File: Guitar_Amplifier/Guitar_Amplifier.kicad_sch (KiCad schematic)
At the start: 11 parts, among them J1 Conn_01x04, J2 Conn_01x02, U1 LM386

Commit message: First version of board layout
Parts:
- C1, C2, C4: footprint (none) -> Capacitor_SMD:C_0603_1608Metric
- C3: footprint (none) -> Capacitor_SMD:CP_Elec_10x10
- D1: footprint (none) -> Diode_SMD:D_0805_2012Metric
- J1: footprint (none) -> Connector_PinHeader_1.00mm:PinHeader_1x04_P1.00mm_Vertical
- J2: footprint (none) -> Connector_PinHeader_1.00mm:PinHeader_1x02_P1.00mm_Vertical
- R1, R2: footprint (none) -> Resistor_SMD:R_0603_1608Metric
- RV1: footprint (none) -> Potentiometer_SMD:Potentiometer_Bourns_TC33X_Vertical; Distributor (none) -> Digikey; Distributor PN (none) -> TC33X-103ETR-ND; Mfg. (none) -> Bourns Inc.; Mfg. PN (none) -> TC33X-2-103E
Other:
- moved on the sheet: C1
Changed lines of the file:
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@@
 	)
 	(junction
-		(at 125.73 57.15)
+		(at 125.73 66.04)
 		(diameter 0)
 		(color 0 0 0 0)
@@
 	(wire
 		(pts
-			(xy 134.62 57.15) (xy 134.62 59.69)
+			(xy 134.62 66.04) (xy 134.62 68.58)
 		)
 		(stroke
@@
 	(wire
 		(pts
-			(xy 134.62 67.31) (xy 134.62 71.12)
+			(xy 134.62 76.2) (xy 134.62 80.01)
 		)
 		(stroke
@@
 	(wire
 		(pts
-			(xy 80.01 74.93) (xy 82.55 74.93)
+			(xy 80.01 74.93) (xy 85.09 74.93)
 		)
 		(stroke
@@
 	(wire
 		(pts
-			(xy 125.73 57.15) (xy 134.62 57.15)
+			(xy 125.73 66.04) (xy 134.62 66.04)
 		)
 		(stroke
@@
 	(wire
 		(pts
-			(xy 125.73 52.07) (xy 125.73 57.15)
+			(xy 125.73 60.96) (xy 125.73 66.04)
 		)
 		(stroke
@@
 	(wire
 		(pts
-			(xy 125.73 57.15) (xy 125.73 81.28)
+			(xy 125.73 66.04) (xy 125.73 81.28)
 		)
 		(stroke
@@
 	(wire
 		(pts
-			(xy 82.55 74.93) (xy 82.55 71.12)
+			(xy 85.09 74.93) (xy 85.09 68.58)
 		)
 		(stroke
@@
 			)
 		)
-		(property "Footprint" ""
+		(property "Footprint" "Resistor_SMD:R_0603_1608Metric"
 			(at 75.946 104.394 90)
 			(effects
@@
 	(symbol
 		(lib_id "power:+9V")
-		(at 125.73 52.07 0)
+		(at 125.73 60.96 0)
 		(unit 1)
 		(exclude_from_sim no)
@@
 		(fields_autoplaced yes)
 		(property "Reference" "#PWR02"
+			(at 125.73 64.77 0)
+			(effects
+				(font
+					(size 1.27 1.27)
+				)
+				(hide yes)
+			)
+		)
+		(property "Value" "+9V"
 			(at 125.73 55.88 0)
 			(effects
@@
 					(size 1.27 1.27)
 				)
-				(hide yes)
-			)
-		)
-		(property "Value" "+9V"
-			(at 125.73 46.99 0)
-			(effects
-				(font
-					(size 1.27 1.27)
-				)
 			)
 		)
 		(property "Footprint" ""
-			(at 125.73 52.07 0)
+			(at 125.73 60.96 0)
 			(effects
 				(font
@@
 		)
 		(property "Datasheet" ""
-			(at 125.73 52.07 0)
+			(at 125.73 60.96 0)
 			(effects
 				(font
@@
 		)
 		(property "Description" "Power symbol creates a global label with name \"+9V\""
-			(at 125.73 52.07 0)
+			(at 125.73 60.96 0)
 			(effects
 				(font
@@
 			)
 		)
-		(property "Footprint" ""
+		(property "Footprint" "Potentiometer_SMD:Potentiometer_Bourns_TC33X_Vertical"
 			(at 101.6 86.36 0)
 			(effects
@@
 		)
 		(property "Description" "Potentiometer, US symbol"
+			(at 101.6 86.36 0)
+			(effects
+				(font
+					(size 1.27 1.27)
+				)
+				(hide yes)
+			)
+		)
+		(property "Mfg." "Bourns Inc."
+			(at 101.6 86.36 0)
+			(effects
+				(font
+					(size 1.27 1.27)
+				)
+				(hide yes)
+			)
+		)
+		(property "Mfg. PN" "TC33X-2-103E"
+			(at 101.6 86.36 0)
+			(effects
+				(font
+					(size 1.27 1.27)
+				)
+				(hide yes)
+			)
+		)
+		(property "Distributor" "Digikey"
+			(at 101.6 86.36 0)
+			(effects
+				(font
+					(size 1.27 1.27)
+				)
+				(hide yes)
+			)
+		)
+		(property "Distributor PN" "TC33X-103ETR-ND"
 			(at 101.6 86.36 0)
 			(effects
@@
 			)
 		)
-		(property "Footprint" ""
+		(property "Footprint" "Diode_SMD:D_0805_2012Metric"
 			(at 74.93 114.3 0)
 			(effects
@@
 			)
 		)
-		(property "Footprint" ""
+		(property "Footprint" "Connector_PinHeader_1.00mm:PinHeader_1x04_P1.00mm_Vertical"
 			(at 74.93 77.47 0)
 			(effects
@@
 			)
 		)
-		(property "Footprint" ""
+		(property "Footprint" "Connector_PinHeader_1.00mm:PinHeader_1x02_P1.00mm_Vertical"
 			(at 168.91 88.9 0)
 			(effects
@@
 			)
 		)
-		(property "Footprint" ""
+		(property "Footprint" "Capacitor_SMD:C_0603_1608Metric"
 			(at 143.8148 92.71 0)
 			(effects
@@
 	(symbol
 		(lib_id "power:+9V")
-		(at 82.55 71.12 0)
+		(at 85.09 68.58 0)
 		(unit 1)
 		(exclude_from_sim no)
@@
 		(fields_autoplaced yes)
 		(property "Reference" "#PWR04"
-			(at 82.55 74.93 0)
+			(at 85.09 72.39 0)
 			(effects
 				(font
@@
 		)
 		(property "Value" "+9V"
-			(at 82.55 66.04 0)
+			(at 85.09 63.5 0)
 			(effects
 				(font
@@
 		)
 		(property "Footprint" ""
-			(at 82.55 71.12 0)
+			(at 85.09 68.58 0)
 			(effects
 				(font
@@
 		)
 		(property "Datasheet" ""
-			(at 82.55 71.12 0)
+			(at 85.09 68.58 0)
 			(effects
 				(font
@@
 		)
 		(property "Description" "Power symbol creates a global label with name \"+9V\""
-			(at 82.55 71.12 0)
+			(at 85.09 68.58 0)
 			(effects
 				(font
@@
 	(symbol
 		(lib_id "Device:C")
-		(at 134.62 63.5 0)
+		(at 134.62 72.39 0)
 		(unit 1)
 		(exclude_from_sim no)
@@
 		(fields_autoplaced yes)
 		(property "Reference" "C1"
-			(at 138.43 62.2299 0)
+			(at 138.43 71.1199 0)
 			(effects
 				(font
@@
 		)
 		(property "Value" "0.1uF"
-			(at 138.43 64.7699 0)
+			(at 138.43 73.6599 0)
 			(effects
 				(font
@@
 			)
 		)
-		(property "Footprint" ""
-			(at 135.5852 67.31 0)
+		(property "Footprint" "Capacitor_SMD:C_0603_1608Metric"
+			(at 135.5852 76.2 0)
 			(effects
 				(font
@@
 		)
 		(property "Datasheet" "~"
-			(at 134.62 63.5 0)
+			(at 134.62 72.39 0)
 			(effects
 				(font
@@
 		)
 		(property "Description" "CAP CER 0.1UF 25V X7R 0603"
-			(at 134.62 63.5 0)
+			(at 134.62 72.39 0)
 			(effects
 				(font
@@
 		)
 		(property "Mfg." "Samsung Electro-Mechanics"
-			(at 134.62 63.5 0)
+			(at 134.62 72.39 0)
 			(effects
 				(font
@@
 		)
 		(property "Mfg. PN" "CL10B104KA8NNNC"
-			(at 134.62 63.5 0)
+			(at 134.62 72.39 0)
 			(effects
 				(font
@@
 		)
 		(property "Distributor" "Digikey"
-			(at 134.62 63.5 0)
+			(at 134.62 72.39 0)
 			(effects
 				(font
@@
 		)
 		(property "Distributor PN" "1276-1006-2-ND"
-			(at 134.62 63.5 0)
+			(at 134.62 72.39 0)
 			(effects
 				(font
@@
 			)
 		)
-		(property "Footprint" ""
+		(property "Footprint" "Resistor_SMD:R_0603_1608Metric"
 			(at 145.796 108.204 90)
 			(effects
@@
 			)
 		)
-		(property "Footprint" ""
+		(property "Footprint" "Capacitor_SMD:CP_Elec_10x10"
 			(at 154.94 88.9 0)
 			(effects
@@
 	(symbol
 		(lib_id "power:GND")
-		(at 134.62 71.12 0)
+		(at 134.62 80.01 0)
 		(unit 1)
 		(exclude_from_sim no)
@@
 		(fields_autoplaced yes)
 		(property "Reference" "#PWR07"
-			(at 134.62 77.47 0)
+			(at 134.62 86.36 0)
 			(effects
 				(font
@@
 		)
 		(property "Value" "GND"
-			(at 134.62 76.2 0)
+			(at 134.62 85.09 0)
 			(effects
 				(font
@@
 		)
 		(property "Footprint" ""
-			(at 134.62 71.12 0)
+			(at 134.62 80.01 0)
 			(effects
 				(font
@@
 		)
 		(property "Datasheet" ""
-			(at 134.62 71.12 0)
+			(at 134.62 80.01 0)
 			(effects
 				(font
@@
 		)
 		(property "Description" "Power symbol creates a global label with name \"GND\" , ground"
-			(at 134.62 71.12 0)
+			(at 134.62 80.01 0)
 			(effects
 				(font
@@
 			)
 		)
-		(property "Footprint" ""
+		(property "Footprint" "Capacitor_SMD:C_0603_1608Metric"
 			(at 134.62 110.7948 0)
 			(effects

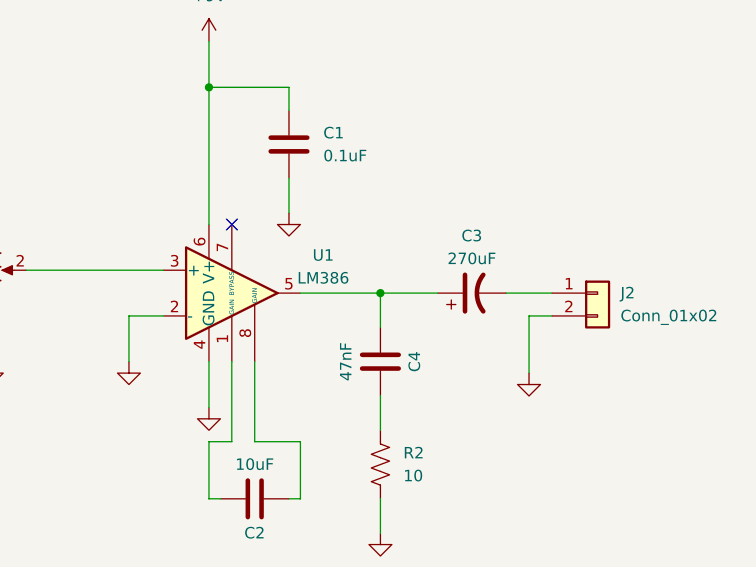
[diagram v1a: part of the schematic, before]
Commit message: Created gerbers, Added GND copper pour
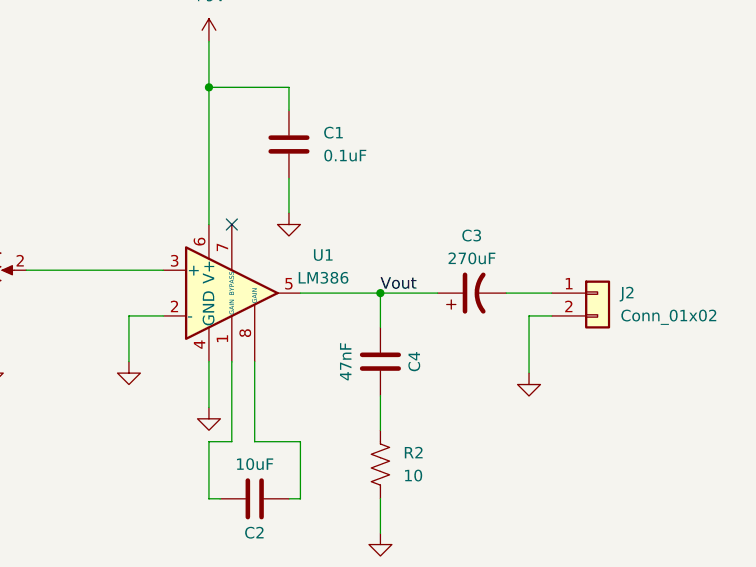
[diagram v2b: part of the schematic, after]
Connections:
- net Vout: now reaches C3.1, C4.2, U1.5
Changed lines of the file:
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@@
+		)
+	)
+	(label "Vout"
+		(at 144.78 88.9 0)
+		(fields_autoplaced yes)
+		(effects
+			(font
+				(size 1.27 1.27)
+			)
+			(justify left bottom)
 		)
 	)

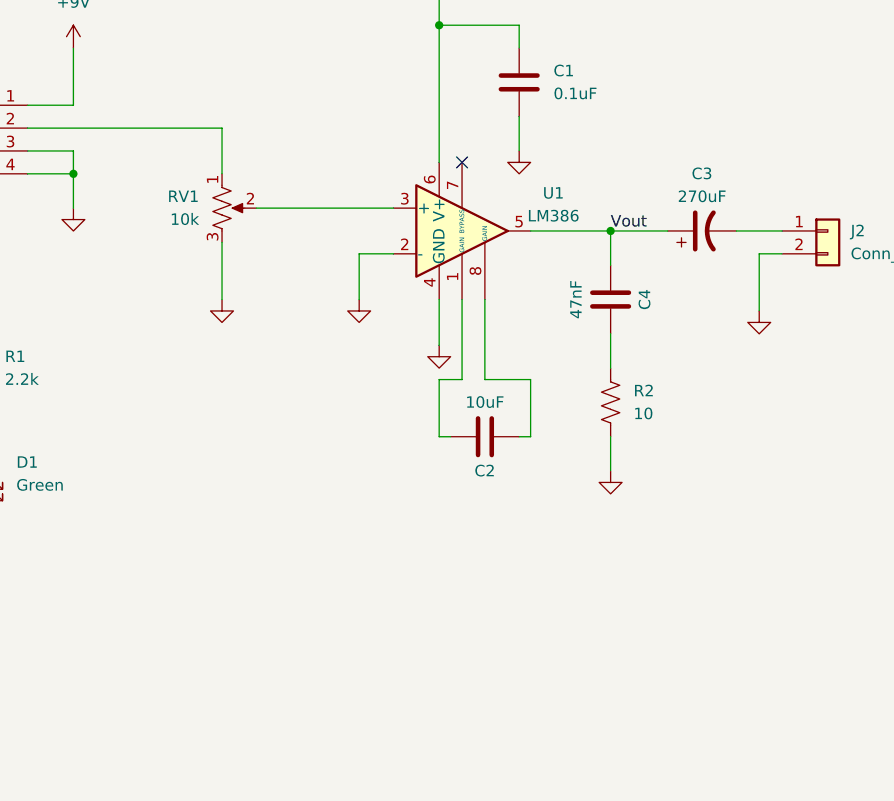
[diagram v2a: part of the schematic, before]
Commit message: Added 3PDT Switch
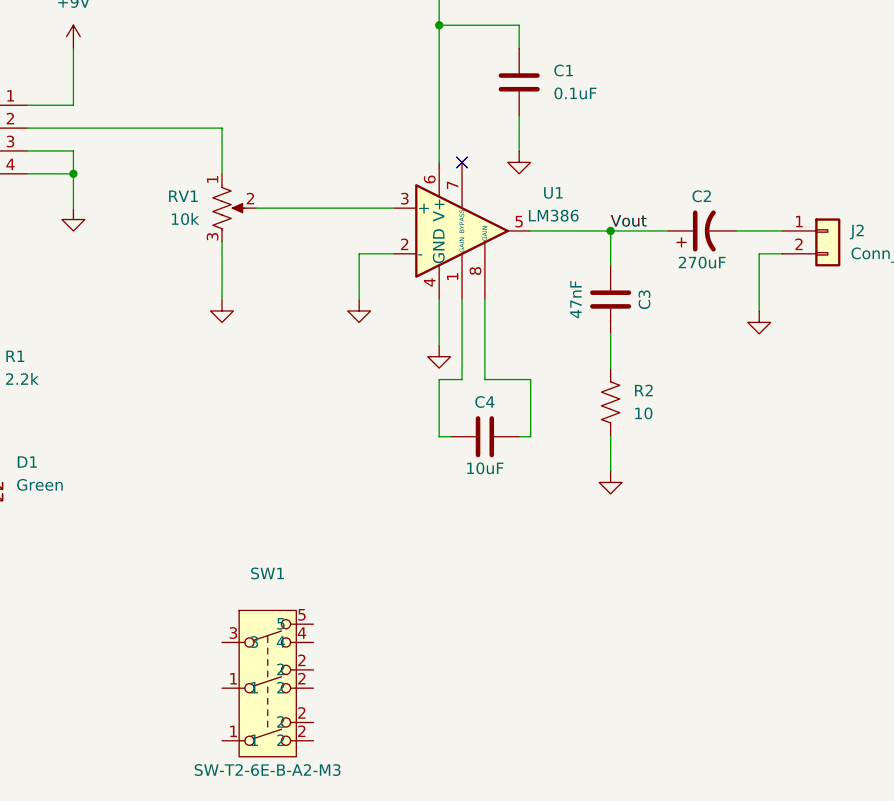
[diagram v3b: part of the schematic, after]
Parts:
- added SW1: ~, symbol RG_Switches:3PDT
- renumbered C3 to C2, C4 to C3, C2 to C4
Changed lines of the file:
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@@
 		(dnp no)
 		(fields_autoplaced yes)
-		(property "Reference" "#PWR011"
+		(property "Reference" "#PWR010"
 			(at 144.78 121.92 0)
 			(effects
@@
 			(project "Guitar_Amplifier"
 				(path "/9d0d146f-8784-4145-96bc-2fe1ea71556f"
-					(reference "#PWR011")
+					(reference "#PWR010")
 					(unit 1)
 				)
@@
 		(dnp no)
 		(fields_autoplaced yes)
-		(property "Reference" "#PWR02"
+		(property "Reference" "#PWR01"
 			(at 125.73 64.77 0)
 			(effects
@@
 			(project "Guitar_Amplifier"
 				(path "/9d0d146f-8784-4145-96bc-2fe1ea71556f"
-					(reference "#PWR02")
+					(reference "#PWR01")
 					(unit 1)
 				)
@@
 		(dnp no)
 		(fields_autoplaced yes)
-		(property "Reference" "#PWR01"
+		(property "Reference" "#PWR09"
 			(at 125.73 107.95 0)
 			(effects
@@
 			(project "Guitar_Amplifier"
 				(path "/9d0d146f-8784-4145-96bc-2fe1ea71556f"
-					(reference "#PWR01")
+					(reference "#PWR09")
 					(unit 1)
 				)
@@
 		(dnp no)
 		(fields_autoplaced yes)
-		(property "Reference" "#PWR05"
+		(property "Reference" "#PWR08"
 			(at 74.93 102.87 0)
 			(effects
@@
 			(project "Guitar_Amplifier"
 				(path "/9d0d146f-8784-4145-96bc-2fe1ea71556f"
-					(reference "#PWR05")
+					(reference "#PWR08")
 					(unit 1)
 				)
@@
 		(dnp no)
 		(fields_autoplaced yes)
-		(property "Reference" "#PWR09"
+		(property "Reference" "#PWR06"
 			(at 116.84 102.87 0)
 			(effects
@@
 			(project "Guitar_Amplifier"
 				(path "/9d0d146f-8784-4145-96bc-2fe1ea71556f"
-					(reference "#PWR09")
+					(reference "#PWR06")
 					(unit 1)
 				)
@@
 		(dnp no)
 		(fields_autoplaced yes)
-		(property "Reference" "#PWR06"
+		(property "Reference" "#PWR011"
 			(at 74.93 129.54 0)
 			(effects
@@
 			(project "Guitar_Amplifier"
 				(path "/9d0d146f-8784-4145-96bc-2fe1ea71556f"
-					(reference "#PWR06")
+					(reference "#PWR011")
 					(unit 1)
 				)
@@
 		(dnp no)
 		(fields_autoplaced yes)
-		(property "Reference" "#PWR08"
+		(property "Reference" "#PWR05"
 			(at 101.6 102.87 0)
 			(effects
@@
 			(project "Guitar_Amplifier"
 				(path "/9d0d146f-8784-4145-96bc-2fe1ea71556f"
-					(reference "#PWR08")
+					(reference "#PWR05")
 					(unit 1)
 				)
@@
 		(on_board yes)
 		(dnp no)
-		(property "Reference" "C4"
+		(property "Reference" "C3"
 			(at 148.59 96.52 90)
 			(effects
@@
 			(project "Guitar_Amplifier"
 				(path "/9d0d146f-8784-4145-96bc-2fe1ea71556f"
-					(reference "C4")
+					(reference "C3")
 					(unit 1)
 				)
@@
 		(dnp no)
 		(fields_autoplaced yes)
-		(property "Reference" "#PWR04"
+		(property "Reference" "#PWR02"
 			(at 85.09 72.39 0)
 			(effects
@@
 			(project "Guitar_Amplifier"
 				(path "/9d0d146f-8784-4145-96bc-2fe1ea71556f"
-					(reference "#PWR04")
+					(reference "#PWR02")
 					(unit 1)
 				)
@@
 		(on_board yes)
 		(dnp no)
-		(property "Reference" "C3"
-			(at 154.94 82.55 90)
+		(property "Reference" "C2"
+			(at 154.94 85.09 90)
 			(effects
 				(font
@@
 		)
 		(property "Value" "270uF"
-			(at 154.94 85.09 90)
+			(at 154.94 92.456 90)
 			(effects
 				(font
@@
 			(project "Guitar_Amplifier"
 				(path "/9d0d146f-8784-4145-96bc-2fe1ea71556f"
-					(reference "C3")
+					(reference "C2")
 					(unit 1)
 				)
@@
 		(dnp no)
 		(fields_autoplaced yes)
-		(property "Reference" "#PWR03"
+		(property "Reference" "#PWR04"
 			(at 85.09 92.71 0)
 			(effects
@@
 			(project "Guitar_Amplifier"
 				(path "/9d0d146f-8784-4145-96bc-2fe1ea71556f"
-					(reference "#PWR03")
+					(reference "#PWR04")
+					(unit 1)
+				)
+			)
+		)
+	)
+	(symbol
+		(lib_id "RG_Switches:3PDT")
+		(at 106.68 135.89 0)
+		(unit 1)
+		(exclude_from_sim no)
+		(in_bom yes)
+		(on_board yes)
+		(dnp no)
+		(property "Reference" "SW1"
+			(at 106.68 127 0)
+			(effects
+				(font
+					(size 1.27 1.27)
+				)
+			)
+		)
+		(property "Value" "~"
+			(at 106.68 129.54 0)
+			(effects
+				(font
+					(size 1.27 1.27)
+				)
+			)
+		)
+		(property "Footprint" ""
+			(at 106.68 135.89 0)
+			(effects
+				(font
+					(size 1.27 1.27)
+				)
+				(hide yes)
+			)
+		)
+		(property "Datasheet" "https://app.adam-tech.com/products/download/data_sheet/203453/sw-t2-6x-b-a2-m3-data-sheet.pdf"
+			(at 106.68 135.89 0)
+			(effects
+				(font
+					(size 1.27 1.27)
+				)
+				(hide yes)
+			)
+		)
+		(property "Description" "SWITCH TOGGLE 3PDT 6A 125V"
+			(at 106.68 135.89 0)
+			(effects
+				(font
+					(size 1.27 1.27)
+				)
+				(hide yes)
+			)
+		)
+		(property "Mfg." "Adam Tech"
+			(at 106.68 135.89 0)
+			(effects
+				(font
+					(size 1.27 1.27)
+				)
+				(hide yes)
+			)
+		)
+		(property "Mfg. PN" "SW-T2-6E-B-A2-M3"
+			(at 106.68 148.844 0)
+			(effects
+				(font
+					(size 1.27 1.27)
+				)
+			)
+		)
+		(property "Distributor" "Digikey"
+			(at 106.68 135.89 0)
+			(effects
+				(font
+					(size 1.27 1.27)
+				)
+				(hide yes)
+			)
+		)
+		(property "Distributor PN" "2057-SW-T2-6E-B-A2-M3-ND"
+			(at 106.68 135.89 0)
+			(effects
+				(font
+					(size 1.27 1.27)
+				)
+				(hide yes)
+			)
+		)
+		(pin "2"
+		)
+		(pin "2"
+		)
+		(pin "2"
+		)
+		(pin "1"
+		)
+		(pin "4"
+		)
+		(pin "1"
+		)
+		(pin "3"
+		)
+		(pin "2"
+		)
+		(pin "5"
+		)
+		(instances
+			(project "Guitar_Amplifier"
+				(path "/9d0d146f-8784-4145-96bc-2fe1ea71556f"
+					(reference "SW1")
 					(unit 1)
 				)
@@
 		(dnp no)
 		(fields_autoplaced yes)
-		(property "Reference" "#PWR010"
+		(property "Reference" "#PWR07"
 			(at 161.29 104.14 0)
 			(effects
@@
 			(project "Guitar_Amplifier"
 				(path "/9d0d146f-8784-4145-96bc-2fe1ea71556f"
-					(reference "#PWR010")
+					(reference "#PWR07")
 					(unit 1)
 				)
@@
 		(dnp no)
 		(fields_autoplaced yes)
-		(property "Reference" "#PWR07"
+		(property "Reference" "#PWR03"
 			(at 134.62 86.36 0)
 			(effects
@@
 			(project "Guitar_Amplifier"
 				(path "/9d0d146f-8784-4145-96bc-2fe1ea71556f"
-					(reference "#PWR07")
+					(reference "#PWR03")
 					(unit 1)
 				)
@@
 		(on_board yes)
 		(dnp no)
-		(property "Reference" "C2"
-			(at 130.81 115.57 90)
+		(property "Reference" "C4"
+			(at 130.81 107.95 90)
 			(effects
 				(font
@@
 		)
 		(property "Value" "10uF"
-			(at 130.81 107.95 90)
+			(at 130.81 115.316 90)
 			(effects
 				(font
@@
 			(project "Guitar_Amplifier"
 				(path "/9d0d146f-8784-4145-96bc-2fe1ea71556f"
-					(reference "C2")
-					(unit 1)
-				)
+					(reference "C4")
+					(unit 1)
+				)
